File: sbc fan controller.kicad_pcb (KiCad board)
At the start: 2 copper layers, 46 x 50.9 mm, 37 parts, among them CON1 ISP-6, J1 Conn_01x13, J2 Conn_01x02, J3 Conn_01x04, J4 Conn_01x04, J5 Conn_01x04, J6 Conn_01x03, J7 Audio-Jack-3, J9 Conn_Coaxial, Q1 Q_PMOS_GSD, U1 ATTINY13A-SSU, U2 OP279, U3 4N25

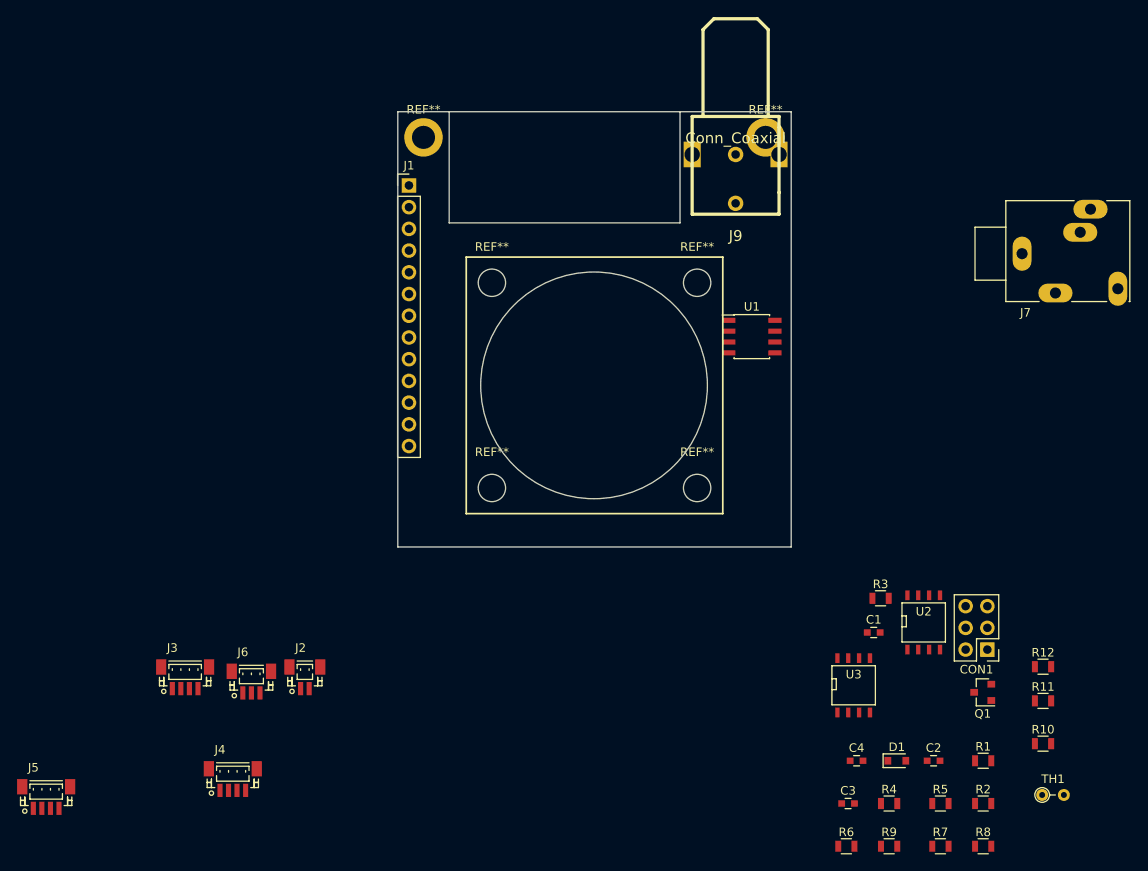
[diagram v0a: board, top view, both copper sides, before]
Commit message: Initial layout of devices
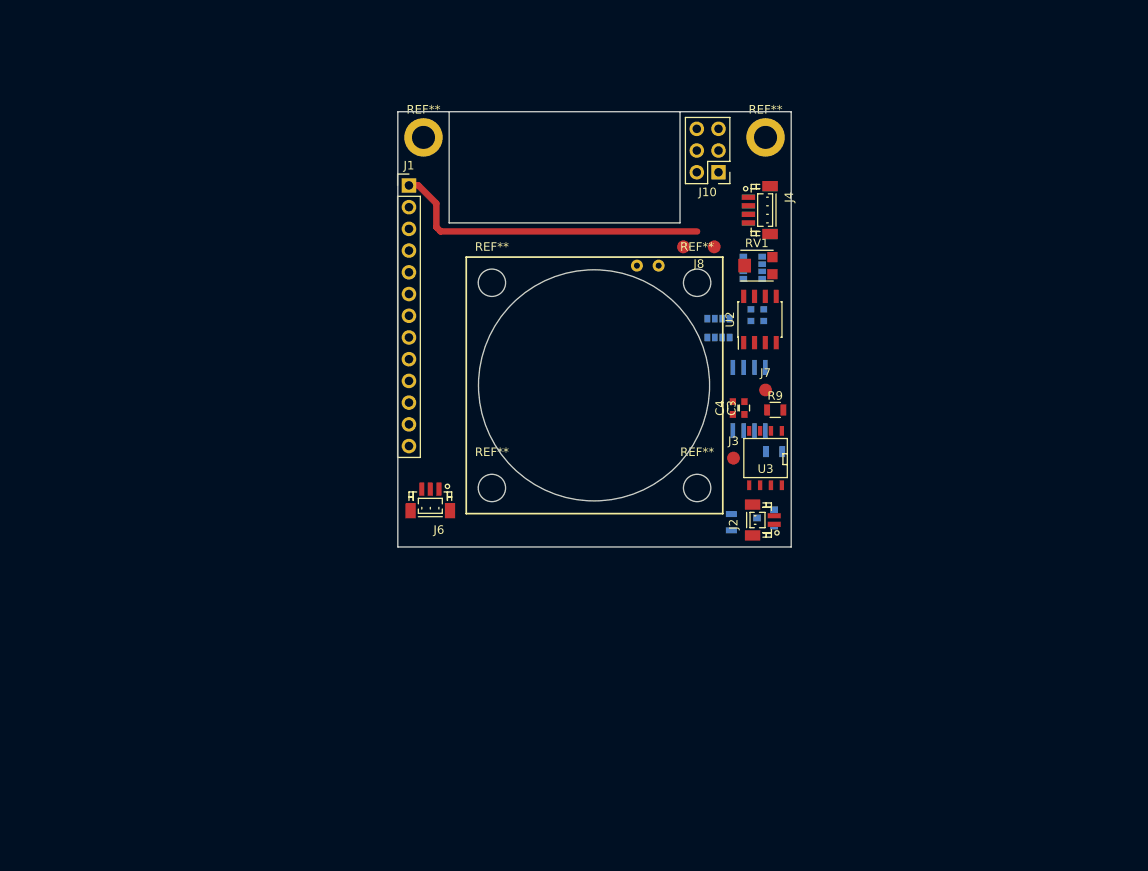
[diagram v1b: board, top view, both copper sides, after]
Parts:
- removed D1: 1N5819, Diodes_SMD:D_0805
- removed J9: Conn_Coaxial, rca:RCA1
- removed R1, R11, R3: 100k, Resistors_SMD:R_0805
- removed R10, R12, R4, R8: 10k, Resistors_SMD:R_0805
- removed R6, R7: 15k, Resistors_SMD:R_0805
- added J8: TEST_2P, node_nrf:Measurement_Point_Round-SMD-2-Pad_Small, F.Cu at (195.2, 55.8)
- added RN1: 100k, node_nrf:YC164J, B.Cu at (201.5, 58.5)
- added RN2: 10k, node_nrf:YC164J, B.Cu at (197.2, 65.3)
- added RV1: 20k, node_nrf:TC33, F.Cu at (202.0, 58.0)
- C1, C2, J5, Q1, R2, R5, TH1: moved to B.Cu
- J3: value Conn_01x04 -> TEST_1P; footprint Connectors_JST:JST_SH_BM04B-SRSS-TB_04x1.00mm_Straight -> Measurement_Points:Measurement_Point_Round-SMD-Pad_Small
- J7: value Audio-Jack-3 -> TEST_1P; footprint Connectors:Stereo_Jack_3.5mm_Switch_Ledino_KB3SPRS -> Measurement_Points:Measurement_Point_Round-SMD-Pad_Small
- R9: value 0 -> 0R
- U1: footprint Housings_SOIC:SOIC-8_3.9x4.9mm_Pitch1.27mm -> Housings_SOIC:SO-8_5.3x6.2mm_Pitch1.27mm; moved to B.Cu
- U2: value OP279 -> LM358; footprint SMD_Packages:SOIC-8-N -> Housings_SOIC:SOIC-8_3.9x4.9mm_Pitch1.27mm
- moved J5 108.0 mm to (202.3, 51.5), turned to 90 degrees
- moved J4 90.7 mm to (202.3, 51.5), turned to 270 degrees
- moved TH1 76.4 mm to (190.5, 58.0), turned to 180 degrees
- moved J3 69.1 mm to (199.2, 80.5)
- moved J10 64.1 mm to (197.5, 47.1)
- moved J2 56.7 mm to (202.8, 87.8), turned to 90 degrees
- moved C2 55.4 mm to (202.0, 64.5)
- moved R9 52.7 mm to (204.1, 74.9)
- moved C3 47.8 mm to (200.5, 74.7), turned to 90 degrees
- moved R5 45.5 mm to (204.0, 79.8), turned to 180 degrees
- moved R2 44.2 mm to (199.0, 88.0), turned to 90 degrees
- moved C4 43.7 mm to (199.2, 74.7), turned to 90 degrees
- moved U2 40.3 mm to (202.3, 64.3), turned to 90 degrees
- moved C1 40.2 mm to (202.0, 63.1)
- moved J7 35.7 mm to (203.0, 72.5)
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- renumbered CON1 to J10
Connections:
- J1 pad 10: /M_BIAS -> Net-(J1-Pad10)
- J1 pad 11: /MIC+ -> Net-(J1-Pad11)
- J1 pad 12: /MIC- -> Net-(J1-Pad12)
- J1 pad 7: (no net) -> Net-(J1-Pad7)
- J1 pad 8: (no net) -> Net-(J1-Pad8)
- J3 pad 1: /MIC+ -> /ISO
- J7 pad 1: (no net) -> /ADJ
- Q1 pad 2: Net-(D1-Pad2) -> /FAN
- TH1 pad 1: /SIG- -> Net-(J8-Pad2)
- U1 pad 2: (no net) -> Net-(U1-Pad2)
- U2 pad 1: /ADJ -> /OP1_OUT
- U2 pad 2: Net-(R1-Pad2) -> /OP1_-
- U2 pad 3: /SIG+ -> /SIG-
- U2 pad 5: /SIG- -> /SIG+
- U2 pad 6: Net-(R11-Pad1) -> /OP2_-
- U2 pad 7: Net-(R4-Pad2) -> /ADJ
- U3 pad 3: (no net) -> Net-(U3-Pad3)
- U3 pad 6: (no net) -> Net-(U3-Pad6)
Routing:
- net +5V: track 0.00 -> 37.6 mm
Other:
- outline, holes or cut-outs redrawn

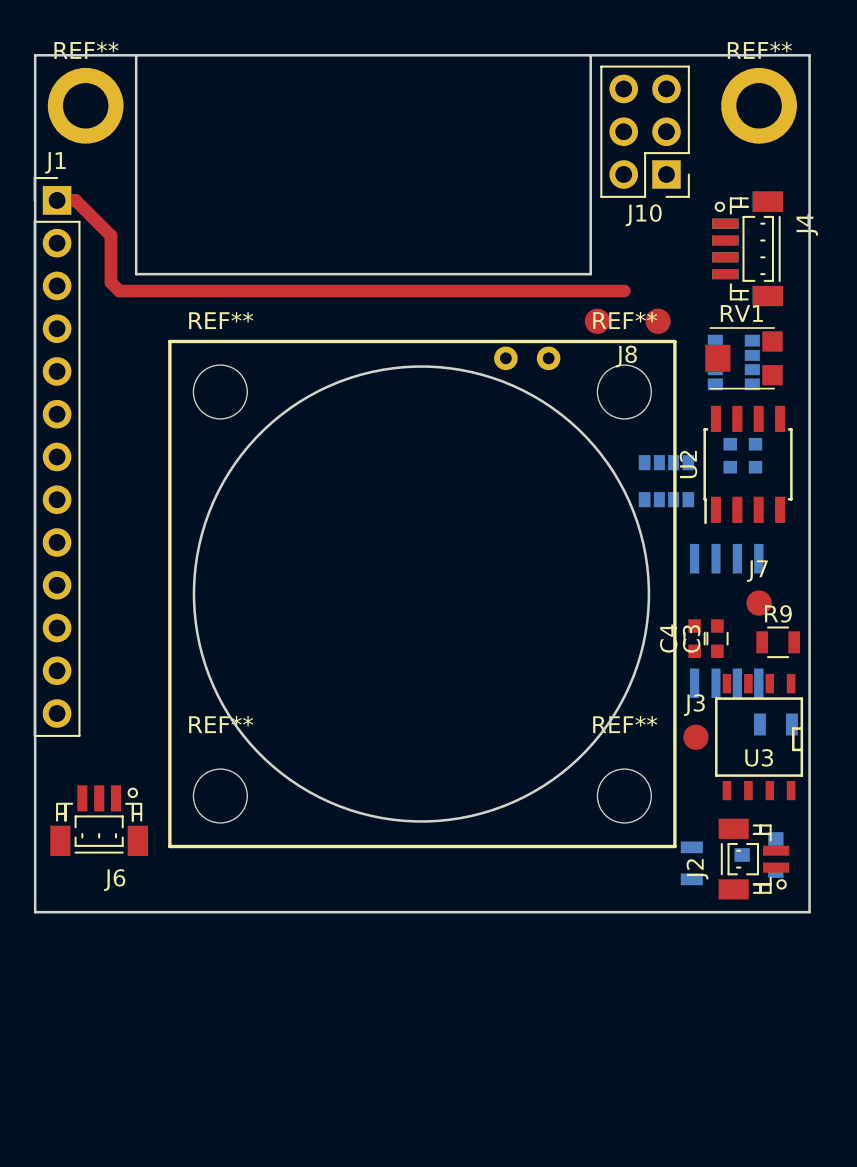
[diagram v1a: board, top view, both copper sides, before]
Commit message: Simplified design, dropped amp; added isolated ground
After testing the dual amp circuit against a simple voltage divider, ADC yields enough resolution to discern heat levels in order to accommodate a look up table for fan speed. Isolated ground plane for switching area included to minimize EMF impact on integrated wifi.
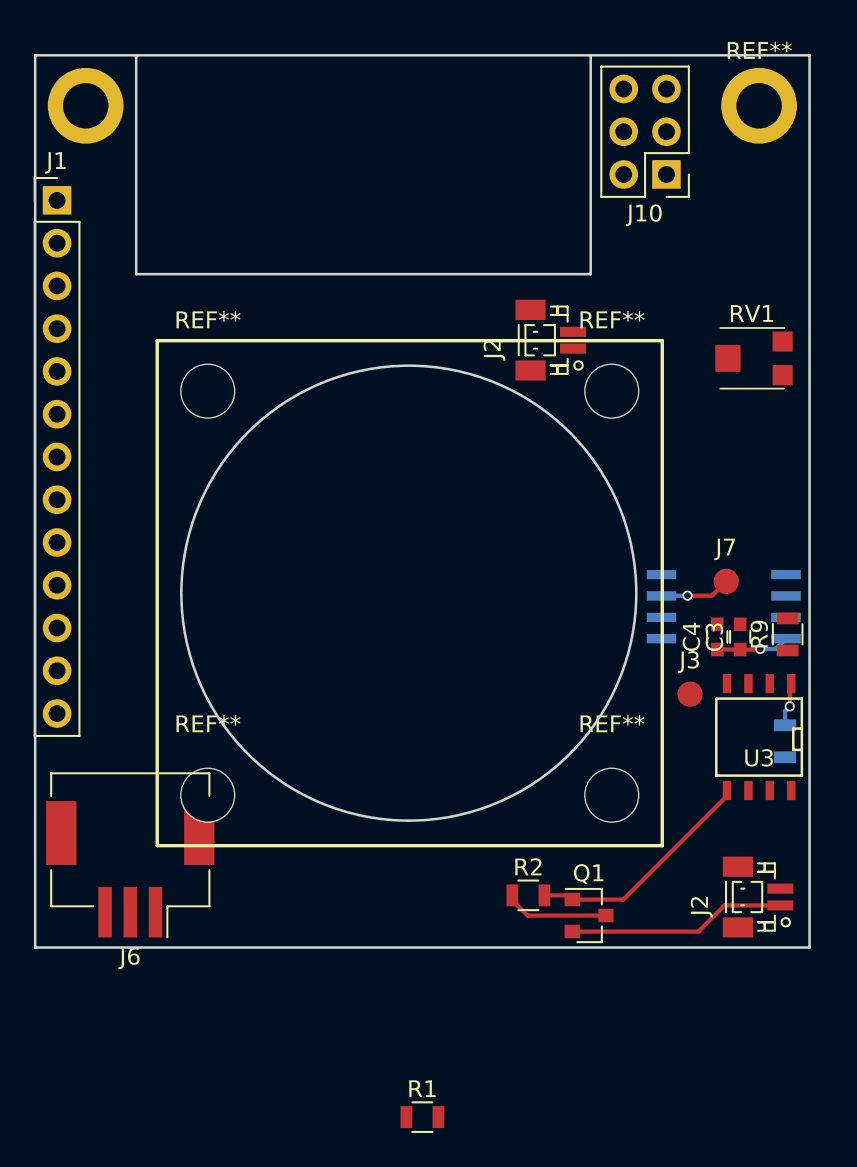
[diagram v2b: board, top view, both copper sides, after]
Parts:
- removed C1: 1uF, Capacitors_SMD:C_0603
- removed C2: 0.1uF, Capacitors_SMD:C_0603
- removed J4, J5: Conn_01x04, Connectors_JST:JST_SH_BM04B-SRSS-TB_04x1.00mm_Straight
- removed J8: TEST_2P, node_nrf:Measurement_Point_Round-SMD-2-Pad_Small
- removed RN1: 100k, node_nrf:YC164J
- removed RN2: 10k, node_nrf:YC164J
- removed TH1: 10k, Resistors_THT:R_Axial_DIN0204_L3.6mm_D1.6mm_P2.54mm_Vertical
- removed U2: LM358, Housings_SOIC:SOIC-8_3.9x4.9mm_Pitch1.27mm
- added J2: Conn_01x02, Connectors_JST:JST_SH_BM02B-SRSS-TB_02x1.00mm_Straight, F.Cu at (190.7, 56.9)
- added R1: 10k, Resistors_SMD:R_0805, F.Cu at (183.0, 103.1)
- J6: footprint Connectors_JST:JST_SH_BM03B-SRSS-TB_03x1.00mm_Straight -> Connectors_JST:JST_ZE_SM03B-ZESS-TB_03x1.5mm_Angled
- Q1, R2: moved to F.Cu
- moved Q1 10.7 mm to (192.9, 91.1), turned to 0 degrees
- moved R2 9.88 mm to (189.3, 89.9), turned to 0 degrees
- moved J6 3.65 mm to (165.7, 88.5)
- moved J3 2.58 mm to (198.9, 78.0)
- moved J7 2.34 mm to (201.1, 71.2)
- moved J2 2.26 mm to (203.0, 90.0)
- moved C4 1.35 mm to (200.5, 74.5)
- moved C3 1.35 mm to (201.9, 74.5)
- moved R5 1.14 mm to (204.6, 80.8), turned to 270 degrees
- moved U1 0.87 mm to (200.9, 72.8), turned to 0 degrees
- moved REF** 0.75 mm to (170.2, 84.0)
- moved REF** 0.75 mm to (194.2, 84.0)
- moved REF** 0.75 mm to (170.2, 60.0)
- moved REF** 0.75 mm to (194.2, 60.0)
- moved R9 0.74 mm to (204.7, 74.4), turned to 90 degrees
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- renumbered REF** to ?
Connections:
- J7 pad 1: /ADJ -> /SIG
- RV1 pad 3: /SIG+ -> /SIG
- U1 pad 3: /ADJ -> /SIG
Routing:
- net +5V: track 37.6 -> 10.6 mm, vias 0 -> 1
- net Net-(Q1-Pad1): track 0.00 -> 13.8 mm
- net /FAN: track 0.00 -> 13.0 mm
- net /SIG: track 0.00 -> 4.21 mm, vias 0 -> 1
- net Net-(R5-Pad1): track 0.00 -> 2.62 mm, vias 0 -> 1
- net /SCK: track 0.00 -> 0.60 mm
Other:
- board size 46 x 50.9 mm -> 46 x 53 mm
